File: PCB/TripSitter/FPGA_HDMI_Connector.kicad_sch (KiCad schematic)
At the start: 16 parts, among them J4 HDMI_A_1.4, U12 TPD12S520DBT

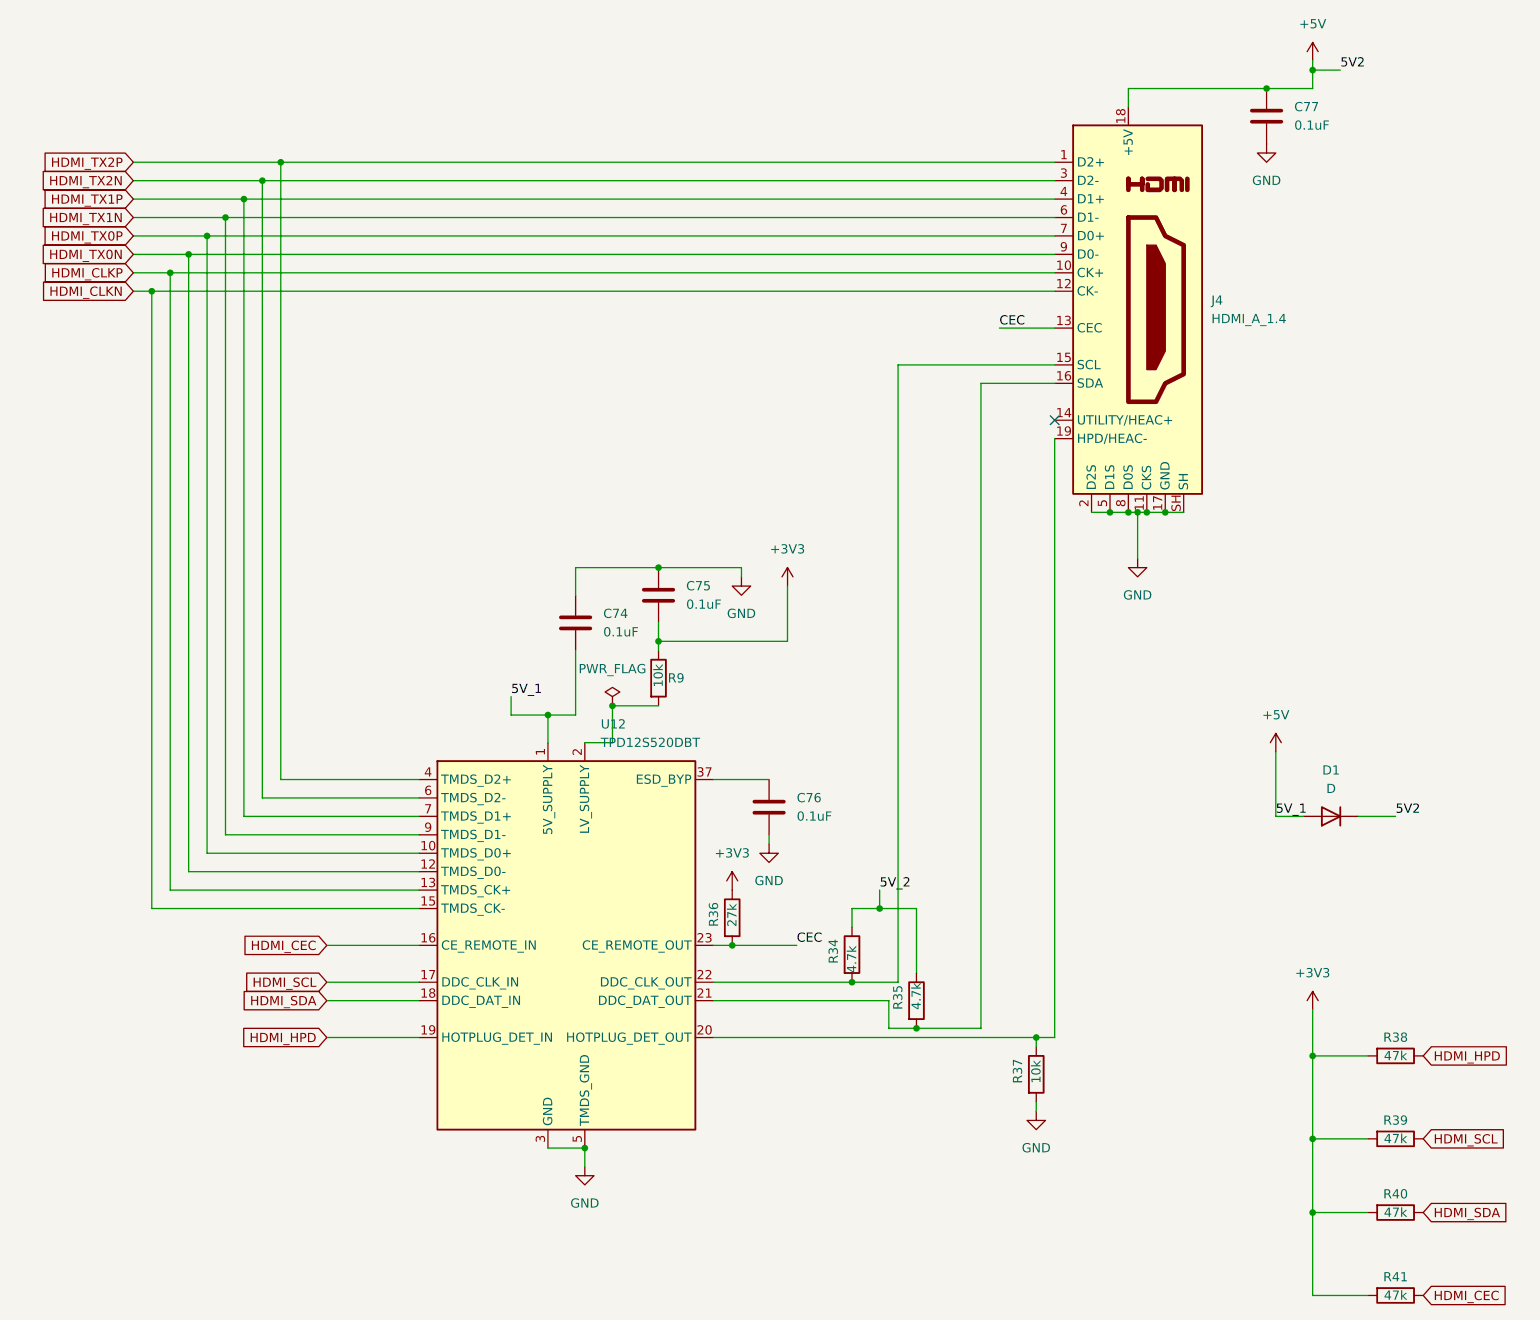
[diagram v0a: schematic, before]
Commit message: pcb: re-structured PCB schematic layout (#17)
Co-authored-by: Sigvart Hovland <sigvart.m@gmail.com>
Co-authored-by: Ida-Sofie Pettersen <idasofie@Ida-Sofies-MacBook-Air.local>
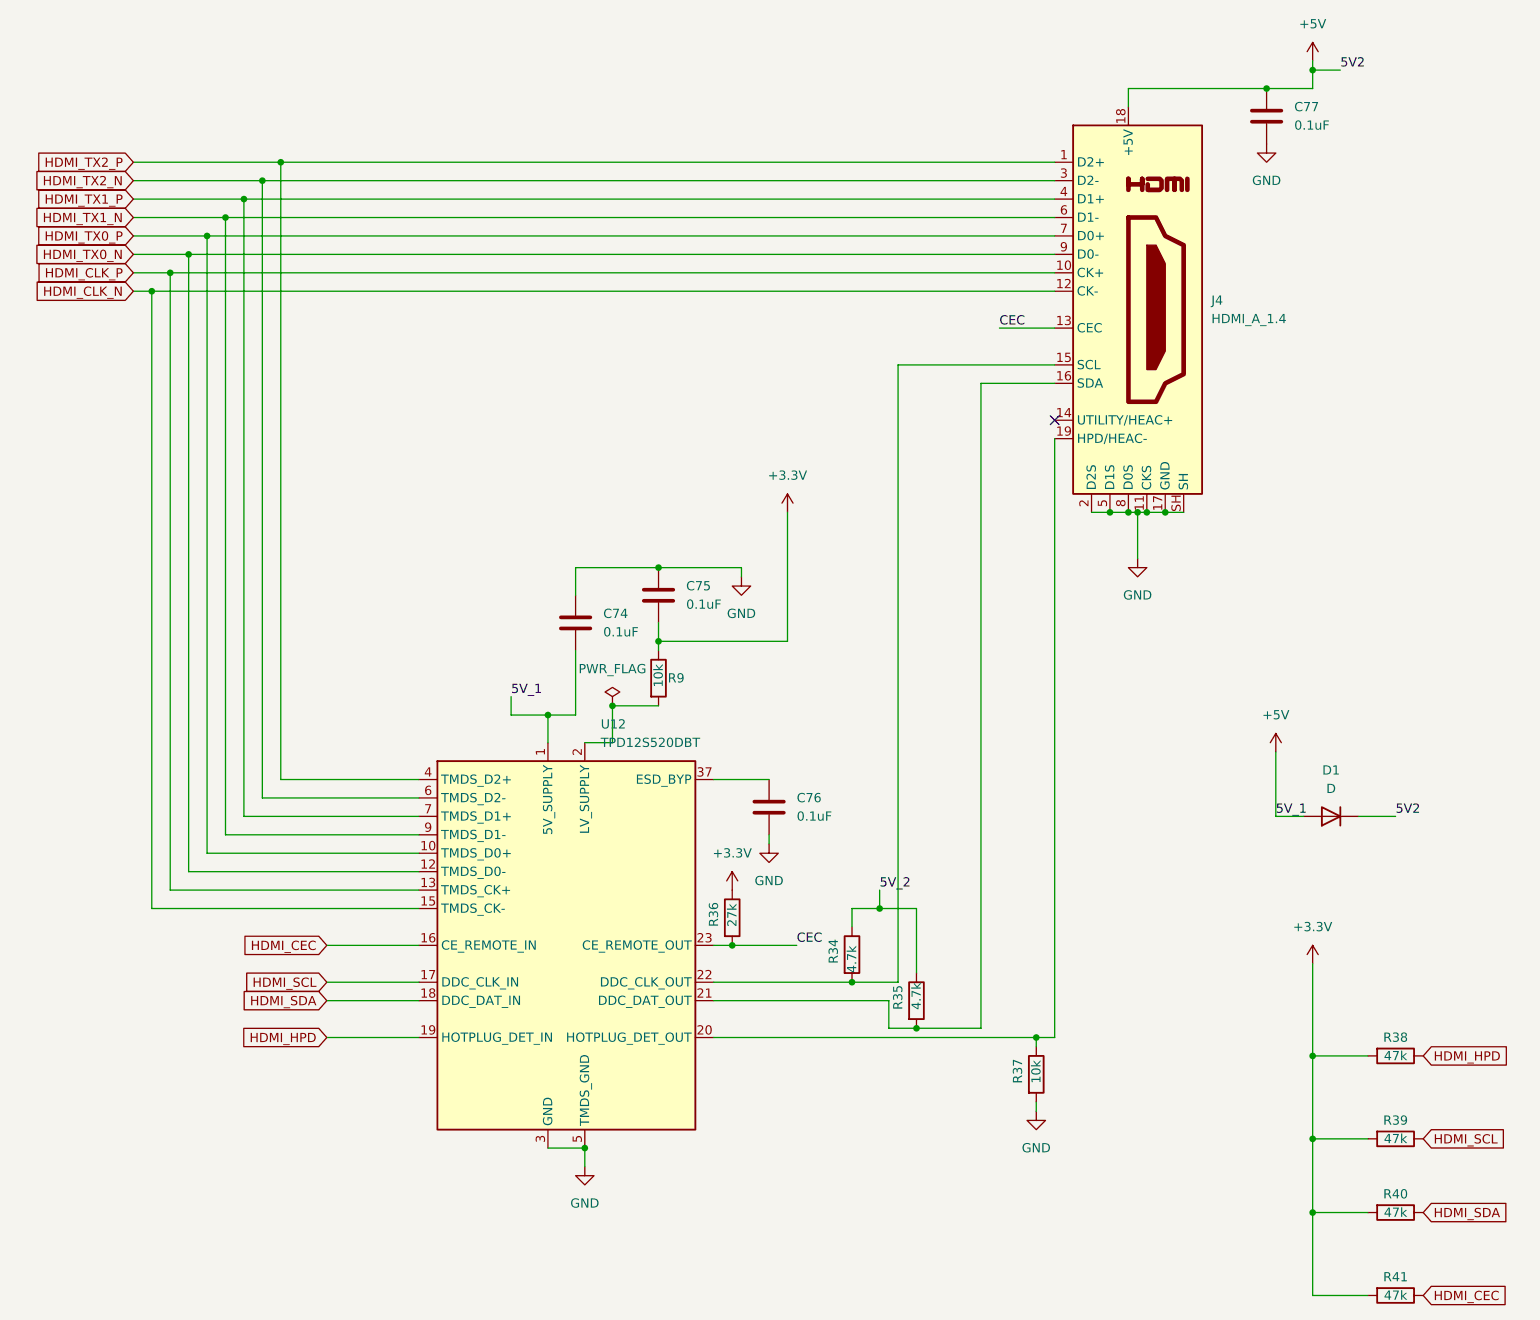
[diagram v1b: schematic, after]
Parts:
- R34, R35, R36: footprint Resistor_SMD:R_0805_2012Metric_Pad1.20x1.40mm_HandSolder -> Resistor_SMD:R_0603_1608Metric_Pad0.98x0.95mm_HandSolder
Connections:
- net +3V3 renamed +3.3V
- net HDMI_CLKN renamed HDMI_CLK_N
- net HDMI_CLKP renamed HDMI_CLK_P
- net HDMI_TX0N renamed HDMI_TX0_N
- net HDMI_TX0P renamed HDMI_TX0_P
- net HDMI_TX1N renamed HDMI_TX1_N
- net HDMI_TX1P renamed HDMI_TX1_P
- net HDMI_TX2N renamed HDMI_TX2_N
- net HDMI_TX2P renamed HDMI_TX2_P
